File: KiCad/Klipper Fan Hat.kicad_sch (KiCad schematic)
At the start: 55 parts, among them J1 GPIO, J2 Serial, J3 I2C, J4 1 Wire, J5 SPI, J6 Vin, Q1 IRLML6344, Q2 IRLML6344, Q3 IRLML6344, Q4 IRLML6344, Q5 IRLML6344, T0 Thermistor, T1 Thermistor, U1 CAT24C256

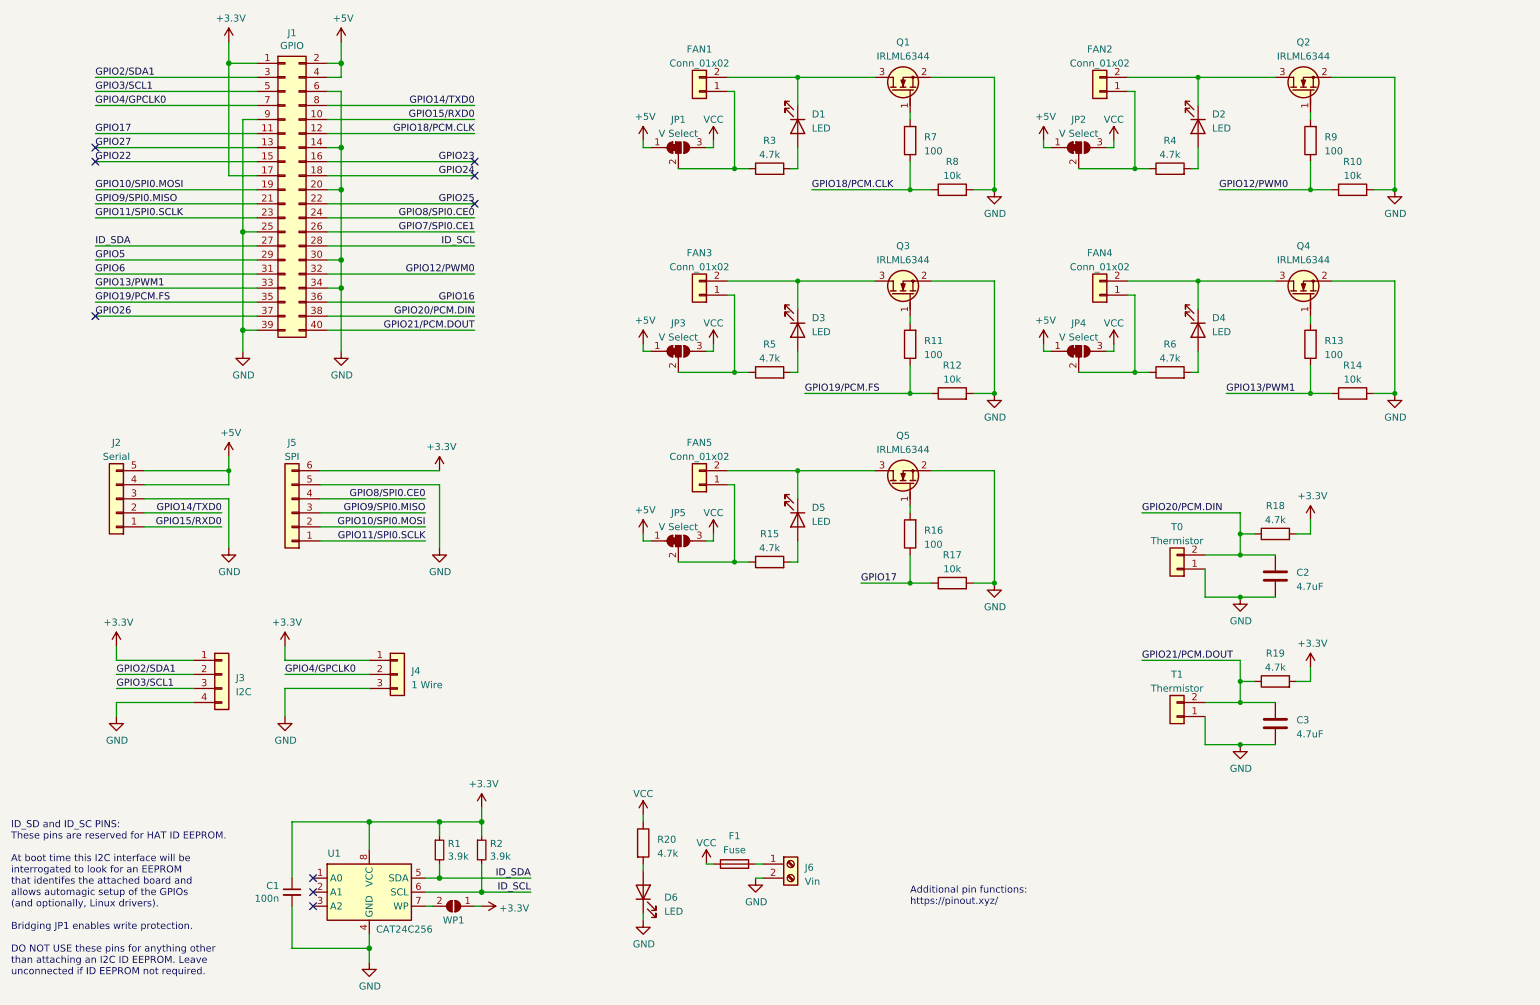
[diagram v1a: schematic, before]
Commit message: Update Klipper Fan Hat to V2
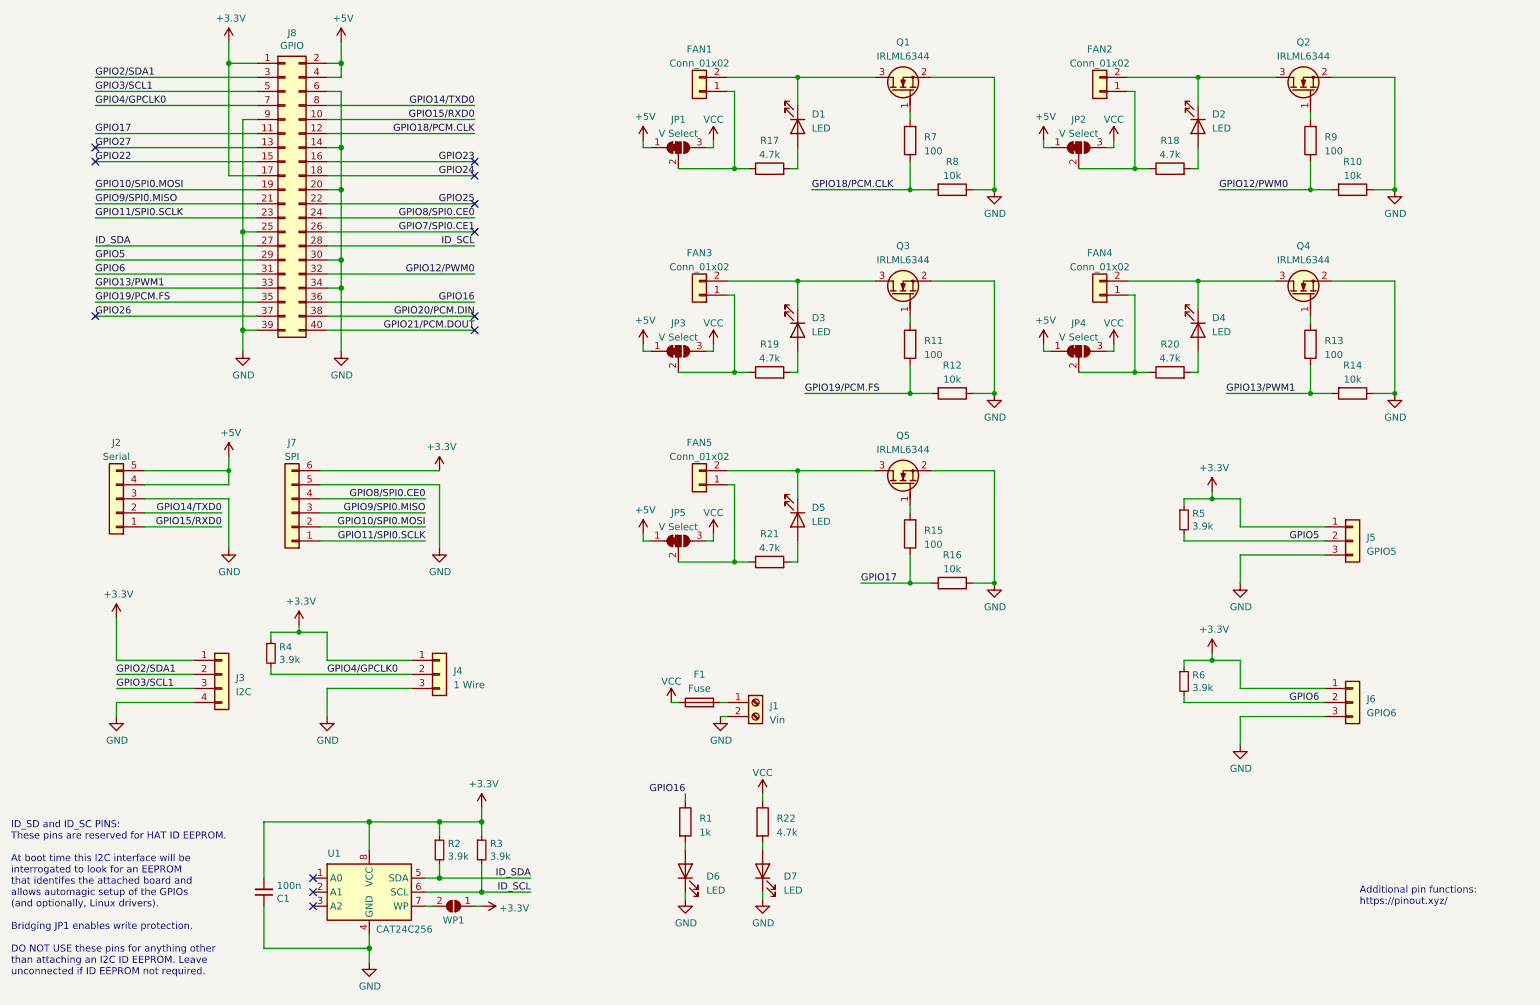
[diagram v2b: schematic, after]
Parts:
- removed C2, C3: 4.7uF, Capacitor_SMD:C_1206_3216Metric, symbol Device:C
- removed R18, R19: 4.7k, Resistor_SMD:R_1206_3216Metric, symbol Device:R
- removed T0, T1: Thermistor, Connector_JST:JST_XH_B2B-XH-A_1x02_P2.50mm_Vertical, symbol Connector_Generic:Conn_01x02
- added D6: LED, LED_SMD:LED_1206_3216Metric_ReverseMount_Hole1.8x2.4mm, symbol Device:LED
- added J5: GPIO5, Connector_JST:JST_XH_B3B-XH-A_1x03_P2.50mm_Vertical, symbol Connector_Generic:Conn_01x03
- added J6: GPIO6, Connector_JST:JST_XH_B3B-XH-A_1x03_P2.50mm_Vertical, symbol Connector_Generic:Conn_01x03
- added R1: 1k, Resistor_SMD:R_1206_3216Metric, symbol Device:R
- added R4, R5, R6: 3.9k, Resistor_SMD:R_1206_3216Metric, symbol Device:R_Small
- renumbered D6 to D7, J6 to J1, J5 to J7, J1 to J8, R16 to R15, R17 to R16, R3 to R17, R4 to R18, R5 to R19, R1 to R2, R6 to R20, R15 to R21, R20 to R22, R2 to R3
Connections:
- net +3V3: now also C1.2, J5.1 (Pin_1), J6.1 (Pin_1), R4.1, R5.1, R6.1; no longer C1.1
- net GND: now also C1.1, R10.1, R12.1, R14.1, R8.1, D6.1 (K), J5.3 (Pin_3), J6.3 (Pin_3); no longer C1.2, R10.2, R12.2, R14.2, R8.2
- net GPIO12/PWM0: now also R10.2; no longer R10.1
- net GPIO13/PWM1: now also R14.2; no longer R14.1
- net GPIO16: now also R1.1
- net GPIO18/PCM.CLK: now also R8.2; no longer R8.1
- net GPIO19/PCM.FS: now also R12.2; no longer R12.1
- net GPIO4/GPCLK0: now also R4.2
- net GPIO5: now also J5.2 (Pin_2), R5.2
- net GPIO6: now also J6.2 (Pin_2), R6.2
- new net: D6.2 (A), R1.2
- no-connect marks 9 -> 12
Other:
- title: (none) -> Klipper Fan Hat
- moved on the sheet: C1, D7, F1, J1, J4, R10, R12, R14, R22, R8
